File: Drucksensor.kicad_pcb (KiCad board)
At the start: 2 copper layers, 99 x 53 mm, 70 parts, among them J101 Conn_01x02, J103 RJ45, J104 RJ45, Q101 Q_NMOS_GSD, Q102 Q_NMOS_GSD, Q103 Q_NMOS_GSD, SW101 SW_SPDT, SW102 SW_SPDT, U101 REF3040, U201 KCSA02-106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

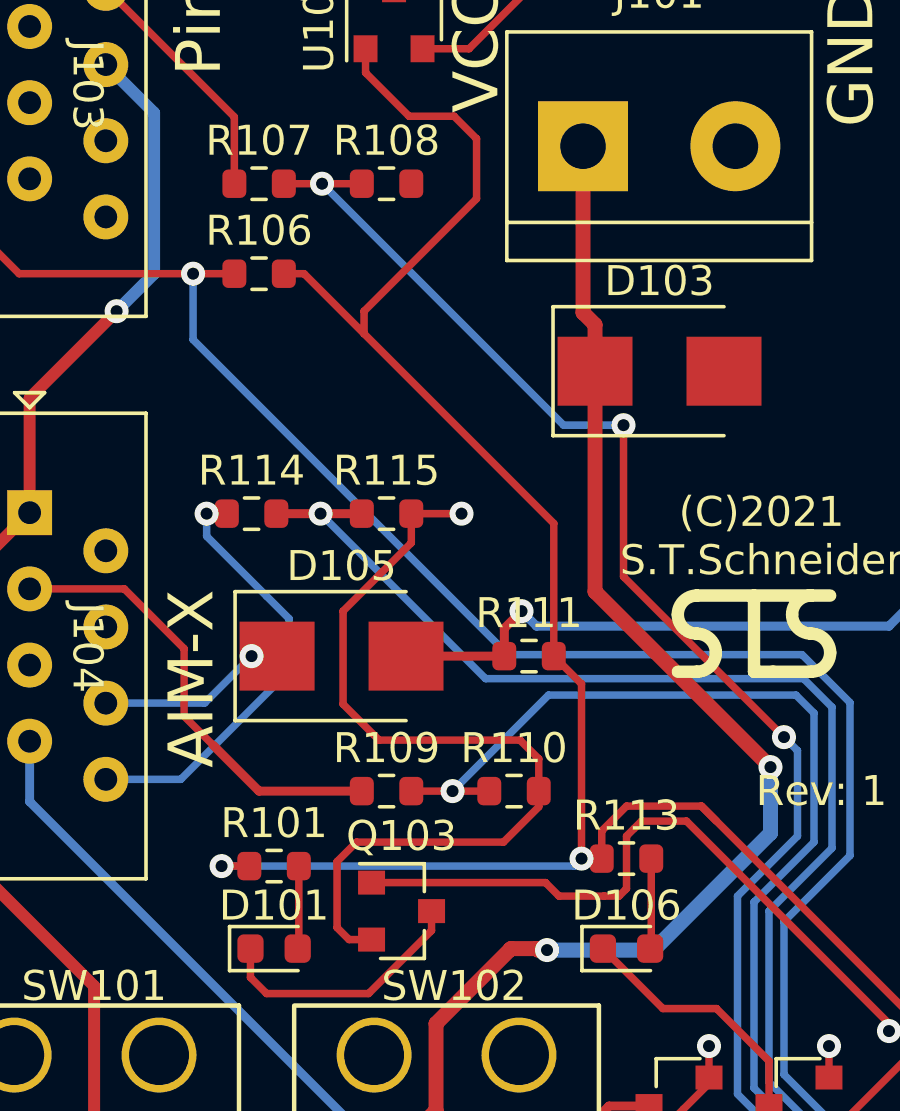
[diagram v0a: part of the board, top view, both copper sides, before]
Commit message: Zweiten Wiederstand zu Spannungsteiler hinzugefügt.
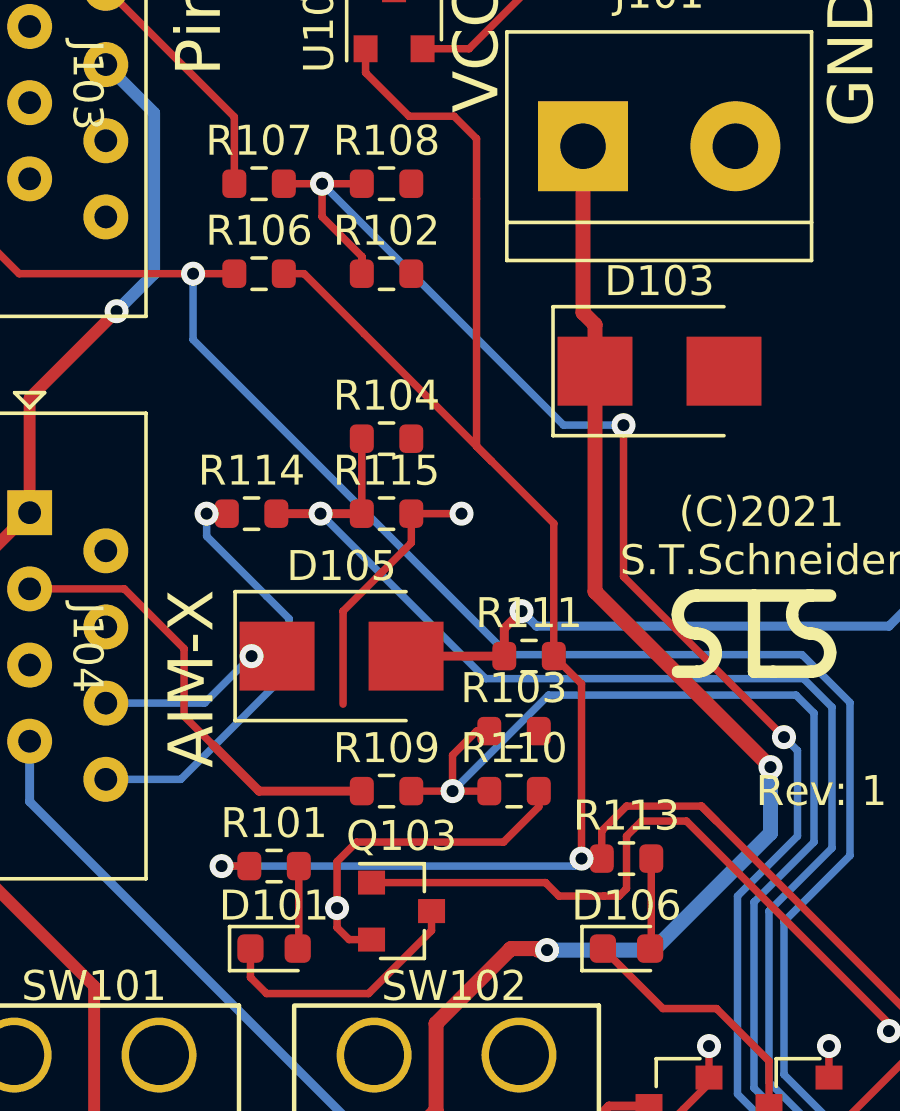
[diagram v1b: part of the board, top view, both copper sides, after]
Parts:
- added R102: 10k, Resistor_SMD:R_0603_1608Metric, F.Cu at (79.8, 33.2)
- added R103: 10k, Resistor_SMD:R_0603_1608Metric, F.Cu at (84.0, 48.5)
- added R104: 10k, Resistor_SMD:R_0603_1608Metric, F.Cu at (79.8, 38.8)
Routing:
- net GND: track 63.4 -> 55.0 mm, vias 15 -> 16
- net /Pirani_ADC: track 68.2 -> 72.1 mm
- net +5V: track 284.7 -> 287.6 mm
- net /Magnetron_ADC: track 58.3 -> 61.1 mm
- net /Magnetron_Setpoint_ADC: track 66.9 -> 69.4 mm

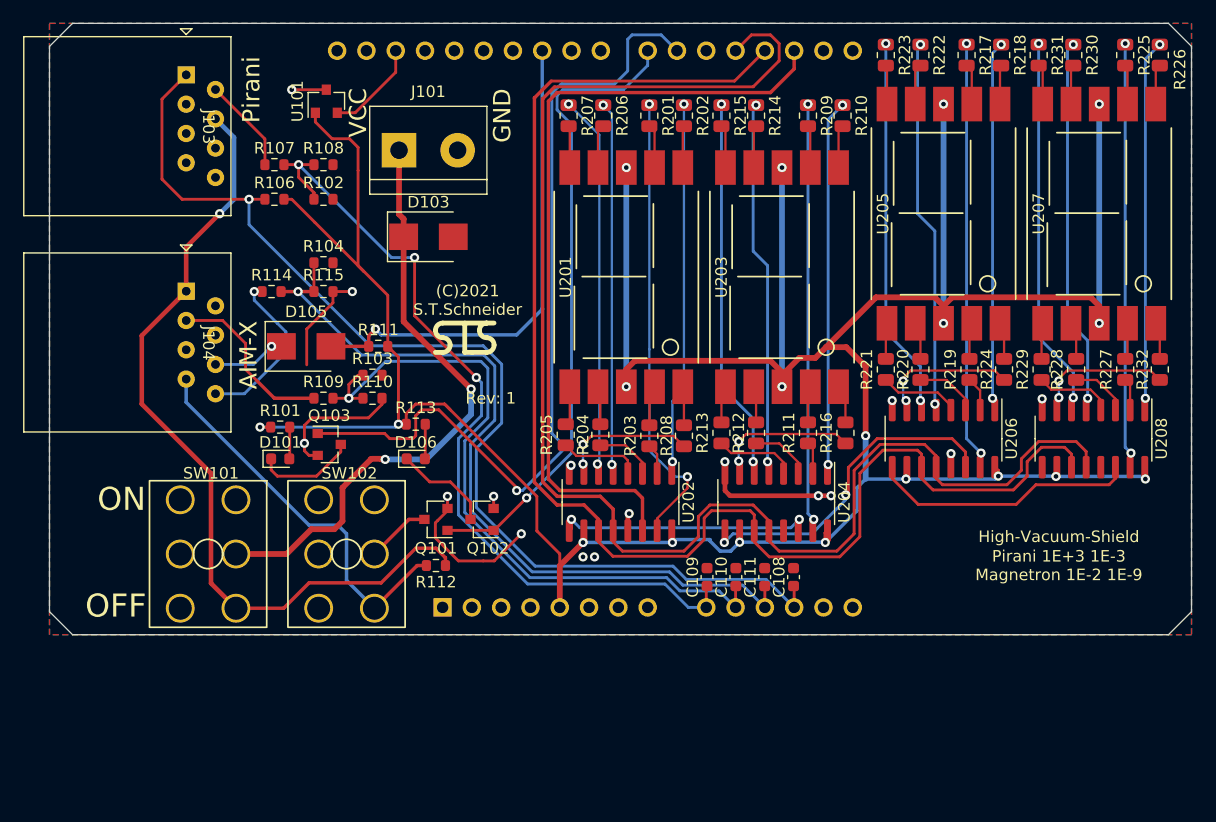
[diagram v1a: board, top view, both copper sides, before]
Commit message: RS232 hinzugefügt
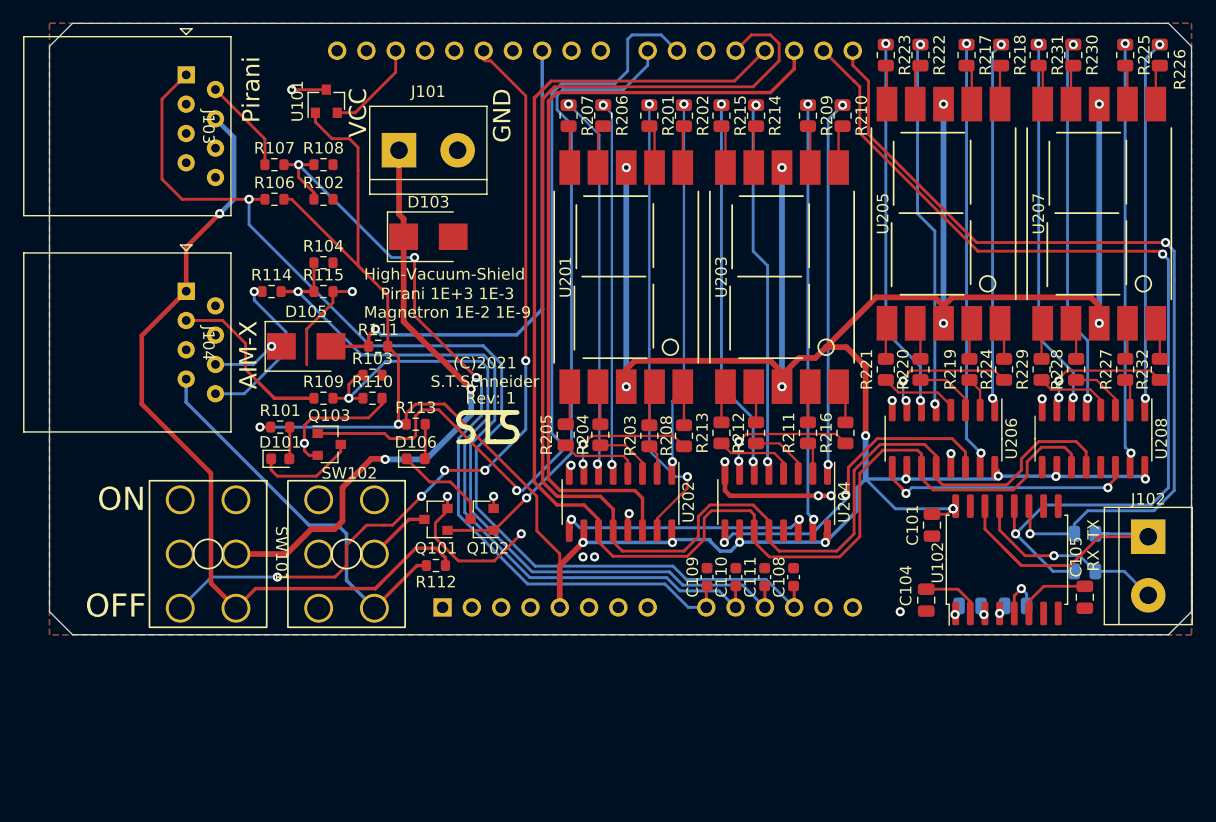
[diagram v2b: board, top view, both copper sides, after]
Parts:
- added C101: 1µ 16V, Capacitor_SMD:C_0805_2012Metric, F.Cu at (132.5, 61.5)
- added C102: 1µ 16V, Capacitor_SMD:C_0805_2012Metric, B.Cu at (135.8, 68.5)
- added C103: 1µ 16V, Capacitor_SMD:C_0805_2012Metric, B.Cu at (139.8, 68.5)
- added C104: 1µ 16V, Capacitor_SMD:C_0805_2012Metric, F.Cu at (132.0, 68.0)
- added C105: 1µ 16V, Capacitor_SMD:C_0805_2012Metric, F.Cu at (145.8, 67.8)
- added J102: Conn_01x02, TerminalBlock:TerminalBlock_bornier-2_P5.08mm, F.Cu at (151.2, 62.5)
- added R105: Open, Resistor_SMD:R_0805_2012Metric, B.Cu at (145.8, 62.2)
- added R116: Open, Resistor_SMD:R_0805_2012Metric, B.Cu at (145.8, 65.5)
- added U102: MAX232, Package_SO:SOIC-16W_7.5x10.3mm_P1.27mm, F.Cu at (139.0, 64.5)
- SW101: value SW_SPDT -> SW_DPST
- moved REF** 8.00 mm to (94.0, 53.6)
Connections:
- A101 pad 15: unconnected-(A101-Pad15) -> /TX
- A101 pad 16: unconnected-(A101-Pad16) -> /RX
- A101 pad 27: unconnected-(A101-Pad27) -> /Main_ON
- SW101 pad 1: unconnected-(SW101-Pad1) -> (no net)
- SW101 pad 5: (no net) -> GND
- SW101 pad 6: (no net) -> /Main_ON
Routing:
- net /RX: track 0.00 -> 83.3 mm, vias 0 -> 2
- net /TX: track 0.00 -> 76.3 mm, vias 0 -> 2
- net /Main_ON: track 0.00 -> 72.2 mm, vias 0 -> 5
- net /RS232_TX: track 0.00 -> 26.4 mm
- net /RS232_RX: track 0.00 -> 17.3 mm, vias 0 -> 1
- net +5V: track 287.6 -> 298.6 mm, vias 19 -> 21
- net Net-(C105-Pad1): track 0.00 -> 6.44 mm
- net Net-(C104-Pad1): track 0.00 -> 5.30 mm
- net Net-(C103-Pad1): track 0.00 -> 4.09 mm, vias 0 -> 1
- net Net-(C103-Pad2): track 0.00 -> 2.01 mm, vias 0 -> 1
- net Net-(C102-Pad2): track 0.00 -> 1.02 mm, vias 0 -> 1
- net Net-(C102-Pad1): track 0.00 -> 0.99 mm, vias 0 -> 1
- net +24V: track 71.1 -> 71.8 mm
- net Net-(U206-Pad9): track 23.2 -> 22.5 mm, vias 0 -> 2
- net GND: vias 16 -> 17
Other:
- board text added: "Bridge for direct RX/TX Open for RS232"
- board text added: "RX TX"
- board text added: "TX RX"

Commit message: Anschluss für Edwards-Turbopumpe hinzugefügt
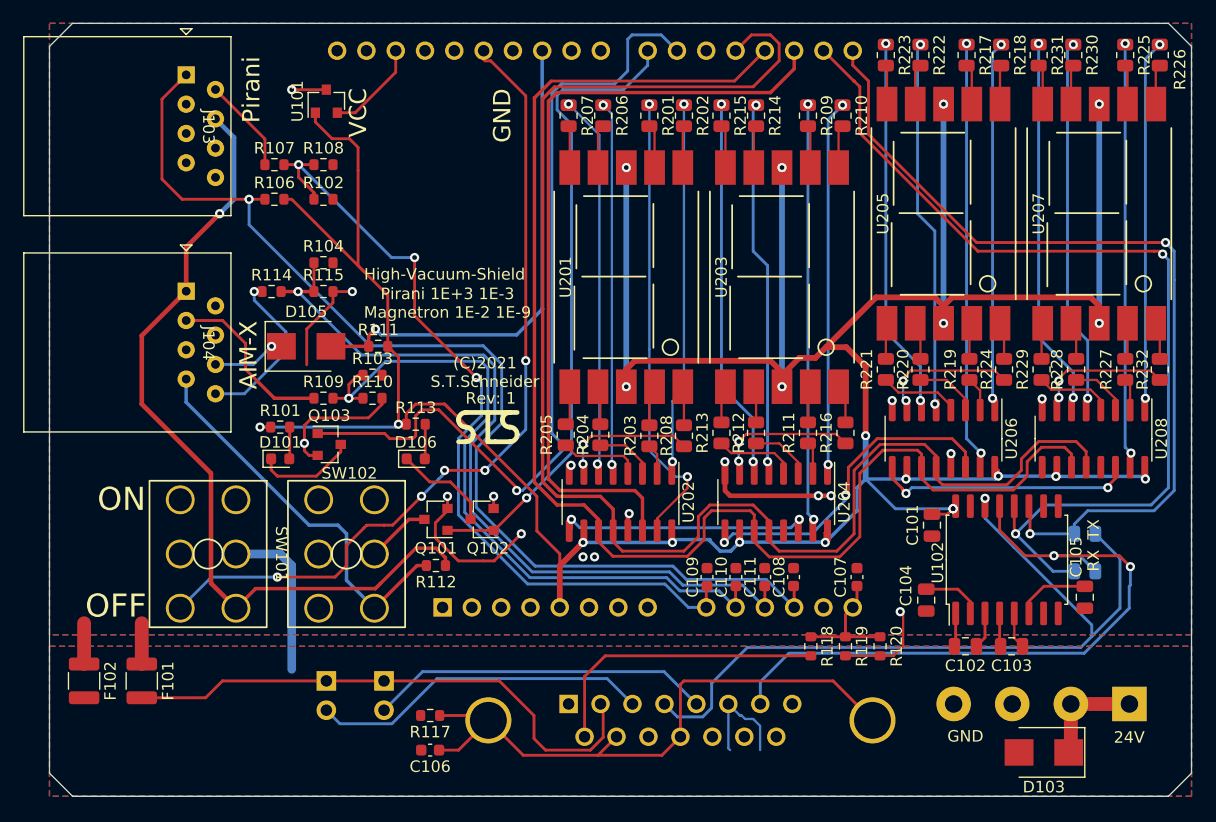
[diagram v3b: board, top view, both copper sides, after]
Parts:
- added C106: 100n, Capacitor_SMD:C_0603_1608Metric, F.Cu at (89.0, 81.0)
- added C107: 100n, Capacitor_SMD:C_0603_1608Metric, F.Cu at (126.0, 66.0)
- added F101: Fuse, Resistor_SMD:R_1210_3225Metric, F.Cu at (64.0, 75.0)
- added F102: Fuse, Resistor_SMD:R_1210_3225Metric, F.Cu at (59.0, 75.0)
- added J105: DB15_Female_MountingHoles, Connector_Dsub:DSUB-15_Female_Vertical_P2.77x2.84mm_MountingHoles, B.Cu at (101.0, 77.0)
- added J106: Serial, Connector_PinSocket_2.54mm:PinSocket_1x02_P2.54mm_Vertical, B.Cu at (85.0, 75.0)
- added R117: 10, Resistor_SMD:R_0603_1608Metric, F.Cu at (89.0, 78.0)
- added R118: 10k, Resistor_SMD:R_0603_1608Metric, F.Cu at (122.0, 72.0)
- added R119: 10k, Resistor_SMD:R_0603_1608Metric, F.Cu at (125.0, 72.0)
- added R120: 10k, Resistor_SMD:R_0603_1608Metric, F.Cu at (128.0, 72.0)
- C102, C103: moved to F.Cu
- J101: footprint TerminalBlock:TerminalBlock_bornier-2_P5.08mm -> TerminalBlock:TerminalBlock_bornier-4_P5.08mm; moved to B.Cu
- J102: value Conn_01x02 -> Start; footprint TerminalBlock:TerminalBlock_bornier-2_P5.08mm -> Connector_PinSocket_2.54mm:PinSocket_1x02_P2.54mm_Vertical; moved to B.Cu
- moved J101 79.5 mm to (149.6, 77.0), turned to 180 degrees
- moved J102 72.3 mm to (80.0, 75.0), turned to 180 degrees
- moved D103 69.6 mm to (142.2, 81.2), turned to 180 degrees
- moved C102 3.52 mm to (135.4, 72.0)
- moved C103 3.52 mm to (139.4, 72.0)
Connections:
- net Net-(D103-Pad1) renamed /24_Ext
- A101 pad 14: unconnected-(A101-Pad14) -> /PumpAnalog_5V
- D103 pad 2: GND -> GNDPWR
- J101 pad 2: GND -> GNDPWR
- J102 pad 1: /RS232_TX -> /GND_Ref
- J102 pad 2: /RS232_RX -> /Start
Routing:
- net Earth: track 0.00 -> 53.3 mm
- net /GND_Ref: track 0.00 -> 48.1 mm
- net /RS232_TX: track 26.4 -> 68.9 mm, vias 0 -> 1
- net /RS232_RX: track 17.3 -> 59.1 mm, vias 1 -> 2
- net /Serial: track 0.00 -> 29.6 mm
- net /Start: track 0.00 -> 29.6 mm
- net /PumpAnalog: track 0.00 -> 25.6 mm
- net /24_Ext: track 52.6 -> 33.3 mm, vias 2 -> 0
- net GND: track 55.0 -> 70.5 mm
- net /PumpAnalog_5V: track 0.00 -> 10.8 mm
- net Net-(C102-Pad1): track 0.99 -> 3.30 mm, vias 1 -> 0
- net Net-(C102-Pad2): track 1.02 -> 3.02 mm, vias 1 -> 0
- net Net-(C103-Pad2): track 2.01 -> 3.28 mm, vias 1 -> 0
- net Net-(C103-Pad1): track 4.09 -> 3.15 mm, vias 1 -> 0
- added copper zone on B.Cu, net /24_Ext
- added copper zone on F.Cu, net GNDPWR
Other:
- board size 99 x 53 mm -> 99 x 67 mm
- board text added: "24V"
- board text added: "24V GND"
- board text added: "Jump_Serial"
- board text added: "Switch_Start"

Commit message: Lüfter Eingefügt
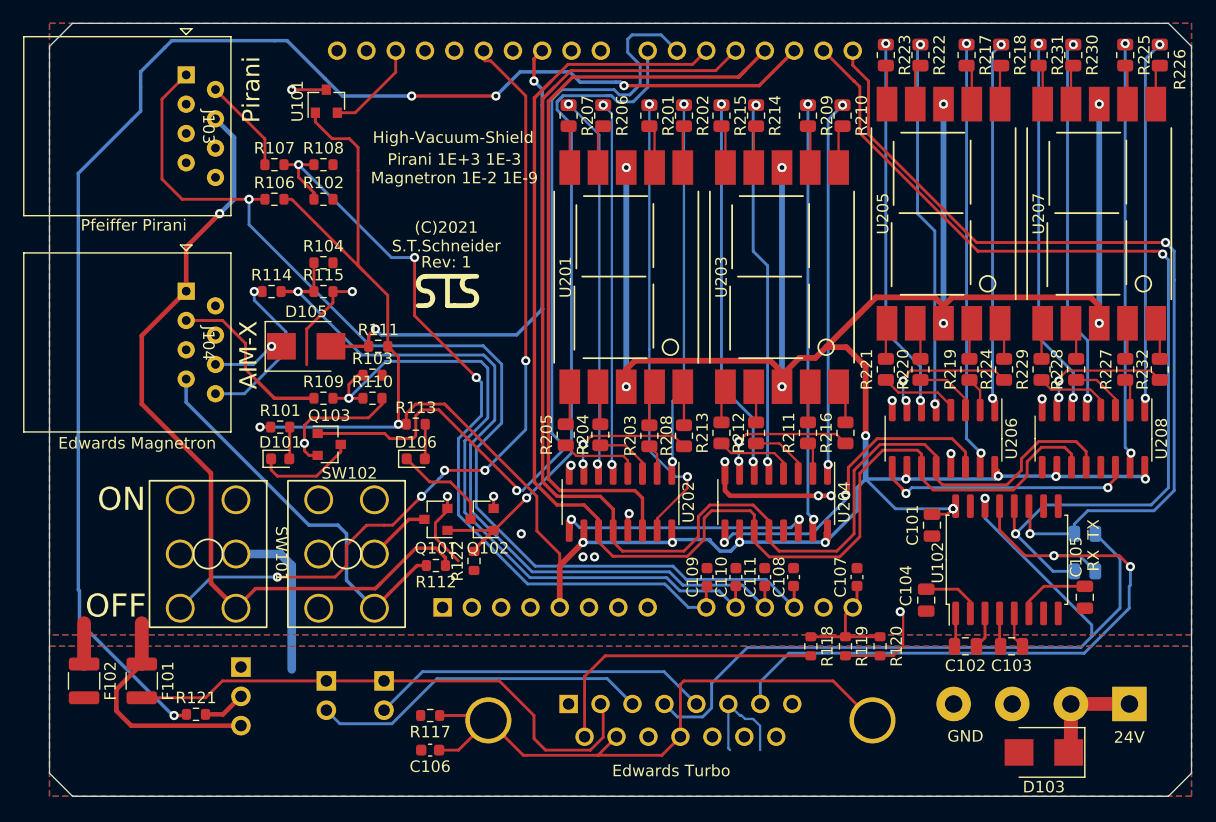
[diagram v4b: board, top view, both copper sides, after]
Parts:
- added J107: Conn_01x03_Male, Connector_PinSocket_2.54mm:PinSocket_1x03_P2.54mm_Vertical, B.Cu at (72.6, 73.8)
- added R121: 10, Resistor_SMD:R_0603_1608Metric, F.Cu at (68.7, 77.9)
- added R122: 10k, Resistor_SMD:R_0603_1608Metric, F.Cu at (92.8, 64.6)
- moved REF** 12.3 mm to (90.5, 41.8)
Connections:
- A101 pad 17: /7SegData -> /Tacho
- A101 pad 18: /7SegClk -> /7SegData
- A101 pad 20: unconnected-(A101-Pad20) -> /7SegClk
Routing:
- net /Tacho: track 0.00 -> 125.0 mm, vias 0 -> 4
- net GND: track 70.5 -> 80.4 mm
- net /7SegEN: track 131.4 -> 121.8 mm
- net /Magnetron_Enable: track 55.3 -> 61.1 mm
- net /7SegClk: track 125.3 -> 120.3 mm
- net Net-(J107-Pad2): track 0.00 -> 3.72 mm
- net /EnableAll: track 74.6 -> 77.7 mm
- net /7SegData: track 68.5 -> 65.9 mm
- net /Magnetron_Trip: track 43.0 -> 43.6 mm, vias 1 -> 2
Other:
- board text added: "Edwards Magnetron"
- board text added: "Edwards Turbo"
- board text added: "Pfeiffer Pirani"
- board text removed: "VCC"

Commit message: Silkscreen angepasst (Lüfter)
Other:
- board text added: "Fan"
- board text added: "Tacho"
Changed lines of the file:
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@@
     (property "Sheetname" "")
     (attr smd)
-    (fp_text reference "R121" (at 0 -1.43) (layer "F.SilkS")
+    (fp_text reference "R121" (at 0 1.5) (layer "F.SilkS")
       (effects (font (size 1 1) (thickness 0.15)))
     )
@@
     (property "Sheetname" "")
     (attr through_hole)
-    (fp_text reference "J107" (at 0 2.77) (layer "B.SilkS")
+    (fp_text reference "J107" (at -2.3 1.7) (layer "B.SilkS")
       (effects (font (size 1 1) (thickness 0.15)) (justify mirror))
     )
@@
   (gr_line (start 56 20) (end 58 18) (layer "Edge.Cuts") (width 0.05))
   (gr_line (start 58 18) (end 153 18) (layer "Edge.Cuts") (width 0.05))
+  (gr_text "Fan" (at 72.6 81.7 90) (layer "B.SilkS")
+    (effects (font (size 1 1) (thickness 0.15)) (justify mirror))
+  )
+  (gr_text "Tacho" (at 68.9 76.3) (layer "B.SilkS")
+    (effects (font (size 1 1) (thickness 0.15)) (justify mirror))
+  )
+  (gr_text "24V" (at 69.7 73.9) (layer "B.SilkS")
+    (effects (font (size 1 1) (thickness 0.15)) (justify mirror))
+  )
   (gr_text "24V   GND" (at 141.9 71.6) (layer "B.SilkS")
     (effects (font (size 2 2) (thickness 0.15)) (justify mirror))
@@
     (effects (font (size 1 1) (thickness 0.15)) (justify mirror))
   )
+  (gr_text "GND\n" (at 69.4 78.9) (layer "B.SilkS")
+    (effects (font (size 1 1) (thickness 0.15)) (justify mirror))
+  )
